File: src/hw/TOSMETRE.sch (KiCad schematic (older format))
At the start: 53 parts, among them J1 Alim, J2 Conn_Coaxial, J3 Conn_01x08_Male, J5 Conn_Coaxial, SW1 SW_Push, SW2 SW_Push_Dual_x2, U1 18F1320, U2 L7805, U3 LT1818, U4 AD5175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

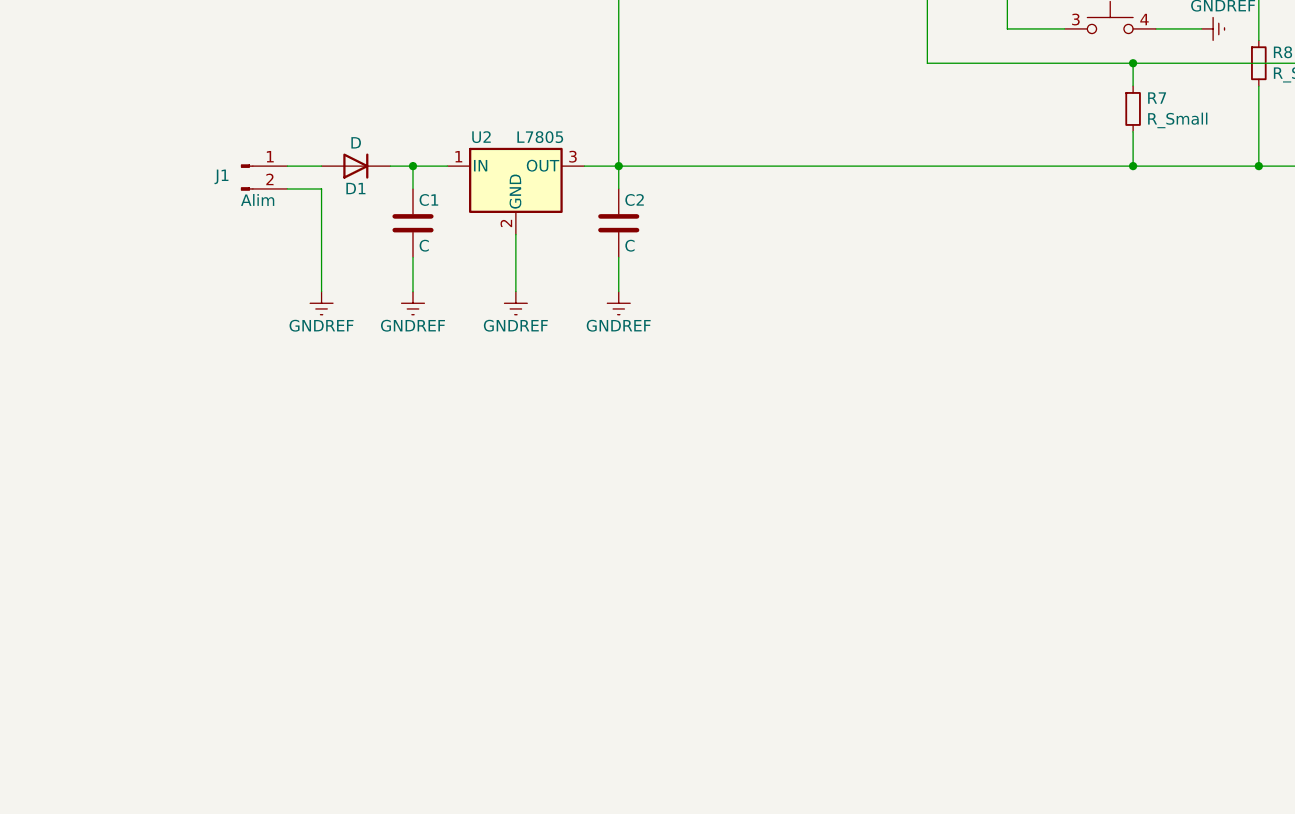
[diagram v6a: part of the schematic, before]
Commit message: #320
Peux tu verifier si le remplacement du 7805 est ok
Dans ce cas je le supprimerai pour ne laisser que le tps709
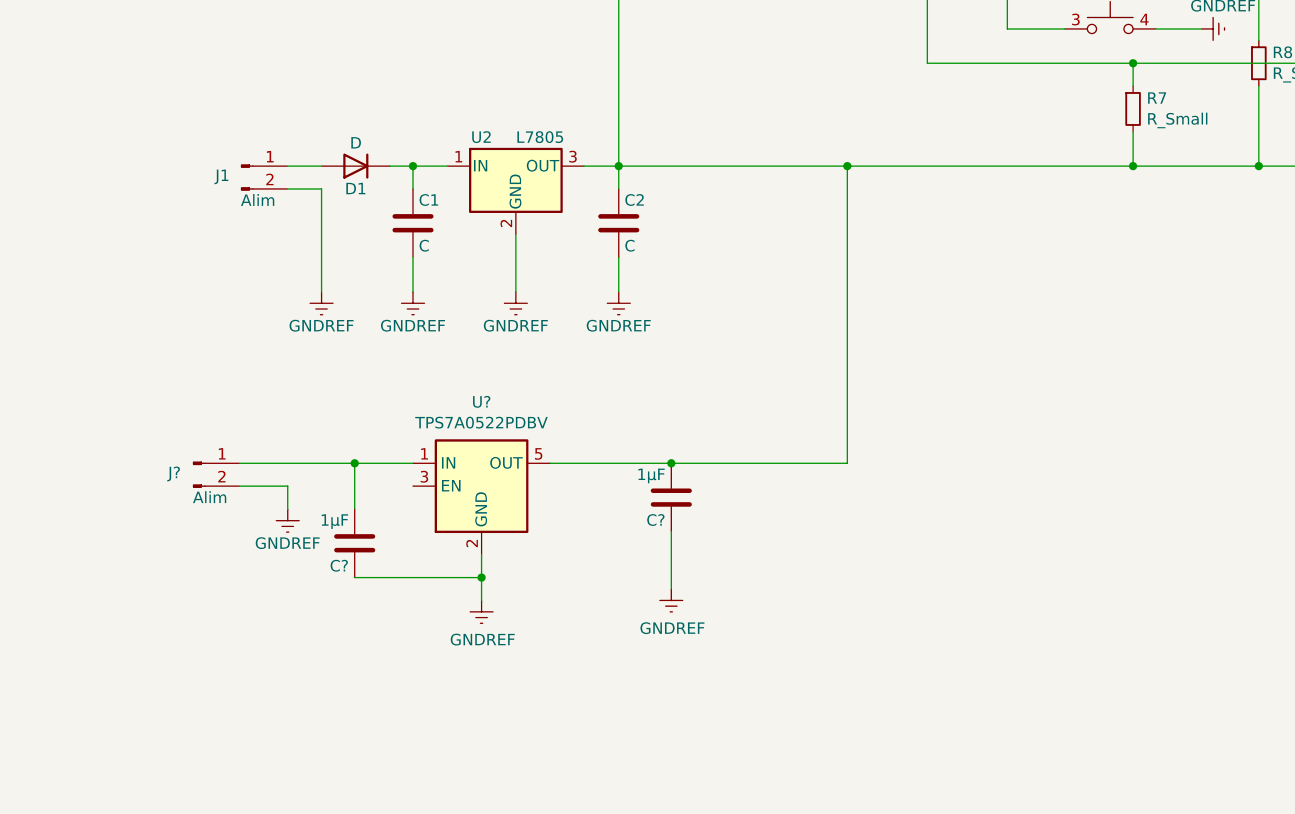
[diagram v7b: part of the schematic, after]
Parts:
- added C? (x2): 1µF, Capacitor_SMD:C_1206_3216Metric, symbol Device:C
- added J?: Alim, Connector_PinHeader_2.54mm:PinHeader_1x02_P2.54mm_Vertical, symbol Connector:Conn_01x02_Male
- added U?: TPS7A0522PDBV, Package_TO_SOT_SMD:SOT-23-5, symbol Regulator_Linear:TPS7A0522PDBV
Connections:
- net GNDREF: now also C?.1, C?.1, J?.2 (Pin_2), U?.2 (GND)
- net at C11.2, C16.2, C17.2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: now also C?.2, U?.5 (OUT)
- new net: C?.2, J?.1 (Pin_1), U?.1 (IN)
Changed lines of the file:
@@
 Connection ~ 5950 8500
 Wire Wire Line
-	3700 8500 5950 8500
+	3700 8500 4700 8500
 Wire Wire Line
 	5050 8050 5950 8050
@@
 Text Notes 8930 2990 0    60   ~ 0
 résistance\ntest ADC1\n
+$Comp
+L Regulator_Linear:TPS7A0522PDBV U?
+U 1 1 6031691C
+P 3100 9900
+F 0 "U?" H 3100 10267 50  0000 C CNN
+F 1 "TPS7A0522PDBV" H 3100 10176 50  0000 C CNN
+F 2 "Package_TO_SOT_SMD:SOT-23-5" H 3100 10250 50  0001 C CNN
+F 3 "https://www.ti.com/lit/ds/symlink/tps7a05.pdf" H 3100 10400 50  0001 C CNN
+	1    3100 9900
+	1    0    0    -1
+$EndComp
+$Comp
+L power:GNDREF #PWR?
+U 1 1 60318E9E
+P 3100 10400
+F 0 "#PWR?" H 3100 10150 50  0001 C CNN
+F 1 "GNDREF" H 3105 10227 50  0000 C CNN
+F 2 "" H 3100 10400 50  0001 C CNN
+F 3 "" H 3100 10400 50  0001 C CNN
+	1    3100 10400
+	1    0    0    -1
+$EndComp
+Wire Wire Line
+	3100 10200 3100 10300
+Wire Wire Line
+	2545 9800 2545 10000
+$Comp
+L Device:C C?
+U 1 1 60384A34
+P 2545 10150
+F 0 "C?" H 2570 10250 50  0000 L CNN
+F 1 "1µF" H 2570 10050 50  0000 L CNN
+F 2 "Capacitor_SMD:C_1206_3216Metric" H 2583 10000 50  0001 C CNN
+F 3 "" H 2545 10150 50  0001 C CNN
+	1    2545 10150
+	-1   0    0    1
+$EndComp
+Wire Wire Line
+	2545 10300 3100 10300
+Connection ~ 3100 10300
+Wire Wire Line
+	3100 10300 3100 10400
+$Comp
+L Device:C C?
+U 1 1 604359F6
+P 3930 9950
+F 0 "C?" H 3955 10050 50  0000 L CNN
+F 1 "1µF" H 3955 9850 50  0000 L CNN
+F 2 "Capacitor_SMD:C_1206_3216Metric" H 3968 9800 50  0001 C CNN
+F 3 "" H 3930 9950 50  0001 C CNN
+	1    3930 9950
+	-1   0    0    1
+$EndComp
+Wire Wire Line
+	4700 8500 4700 9800
+Connection ~ 4700 8500
+Wire Wire Line
+	4700 8500 5950 8500
+$Comp
+L power:GNDREF #PWR?
+U 1 1 604C4E25
+P 2252 10001
+F 0 "#PWR?" H 2252 9751 50  0001 C CNN
+F 1 "GNDREF" H 2252 9851 50  0000 C CNN
+F 2 "" H 2252 10001 50  0001 C CNN
+F 3 "" H 2252 10001 50  0001 C CNN
+	1    2252 10001
+	1    0    0    -1
+$EndComp
+Wire Wire Line
+	2545 9800 2800 9800
+Wire Wire Line
+	2545 9800 2040 9800
+Connection ~ 2545 9800
+$Comp
+L Connector:Conn_01x02_Male J?
+U 1 1 606A489C
+P 1840 9800
+F 0 "J?" H 1757 9758 50  0000 C CNN
+F 1 "Alim" H 1913 9649 50  0000 C CNN
+F 2 "Connector_PinHeader_2.54mm:PinHeader_1x02_P2.54mm_Vertical" H 1840 9800 50  0001 C CNN
+F 3 "~" H 1840 9800 50  0001 C CNN
+	1    1840 9800
+	1    0    0    -1
+$EndComp
+Wire Wire Line
+	2252 9900 2040 9900
+Wire Wire Line
+	2252 9900 2252 10001
+Connection ~ 3930 9800
+Wire Wire Line
+	3930 9800 4700 9800
+Wire Wire Line
+	3400 9800 3930 9800
+$Comp
+L power:GNDREF #PWR?
+U 1 1 608AE8E8
+P 3930 10350
+F 0 "#PWR?" H 3930 10100 50  0001 C CNN
+F 1 "GNDREF" H 3935 10177 50  0000 C CNN
+F 2 "" H 3930 10350 50  0001 C CNN
+F 3 "" H 3930 10350 50  0001 C CNN
+	1    3930 10350
+	1    0    0    -1
+$EndComp
+Wire Wire Line
+	3930 10100 3930 10350
 $EndSCHEMATC

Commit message: oups
c'est de ma faute
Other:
- note added: "résistance\ntest AOP1\n"
- note removed: "résistance\ntest ADC1\n"
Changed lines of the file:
@@
 $EndComp
 Text Notes 9920 9090 0    60   ~ 0
-résistance\ntest ADC1\n
+résistance\ntest AOP1\n
 Text Notes 8930 2990 0    60   ~ 0
-résistance\ntest ADC1\n
+résistance\ntest AOP1\n
 $Comp
 L Regulator_Linear:TPS7A0522PDBV U?
